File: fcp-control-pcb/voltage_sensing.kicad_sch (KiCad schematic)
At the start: 143 parts, among them J13 Conn_01x10_Male, J14 Conn_01x10_Male, J15 Conn_01x10_Male, U10 LM2902, U11 LM2902, U12 LM2902, U13 CD74HC4067SM, U14 CD74HC4067SM, U5 LM2902, U6 LM2902, U7 LM2902, U8 LM2902, U9 LM2902

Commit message: queen r1.1
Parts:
- removed C13, C14, C15, C16, C17, C18, C19, C20, C21, C22: 0.1 uF, Capacitor_SMD:C_0805_2012Metric_Pad1.18x1.45mm_HandSolder, symbol Device:C
- removed R10, R106, R107, R108, R109, R11, R110, R111, R112, R113, R114, R115, R116, R117, R12, R13, R14, R15, R16, R17, R18, R19, R20, R21, R22, R23, R24, R25, R42, R43, R44, R45, R46, R47, R48, R49, R50, R51, R52, R53, R54, R55, R56, R57, R74, R75, R76, R77, R78, R79, R80, R81, R82, R83, R84, R85, R86, R87, R88, R89: 20k, Resistor_SMD:R_0402_1005Metric_Pad0.72x0.64mm_HandSolder, symbol Device:R
- removed R100, R101, R102, R103, R104, R105, R118, R119, R120, R121, R122, R123, R124, R125, R126, R127, R128, R129, R26, R27, R28, R29, R30, R31, R32, R33, R34, R35, R36, R37, R38, R39, R40, R41, R58, R59, R60, R61, R62, R63, R64, R65, R66, R67, R68, R69, R70, R71, R72, R73, R90, R91, R92, R93, R94, R95, R96, R97, R98, R99: 91k, Resistor_SMD:R_0402_1005Metric_Pad0.72x0.64mm_HandSolder, symbol Device:R
- removed U10, U11, U12, U5, U6, U7, U8, U9: LM2902, Package_SO:SOIC-14_3.9x8.7mm_P1.27mm, symbol Amplifier_Operational:LM2902
- removed U13, U14: CD74HC4067SM, Package_SO:SSOP-24_5.3x8.2mm_P0.65mm, symbol 74xx:CD74HC4067SM
- added C? (x2): (no value), symbol Device:C_Small
- added J?: (no value), symbol Connector:Conn_01x02_Male
- added RN? (x2): (no value), symbol Device:R_Pack08
- added RN? (x3): 3.3k, Package_SO:SOIC-16_4.55x10.3mm_P1.27mm, symbol Device:R_Pack08
- added RN? (x3): 1k, Package_SO:SOIC-16_4.55x10.3mm_P1.27mm, symbol Device:R_Pack08
- added U? (x3): ADC1283, Package_SO:TSSOP-16_4.4x5mm_P0.65mm, symbol Custom:ADC1283
- added U?: (no value), symbol Custom:AS78L05RTR-G1
- added U?: (no value), symbol Custom:ADC1283
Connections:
- net +5V: now also U?.13 (DVCC), U?.13 (DVCC), U?.13 (DVCC), U?.13 (DVCC)
- net GND: now also C?.2, C?.2, U?.12 (DGND), U?.12 (DGND), U?.12 (DGND), U?.2 (GND), U?.3 (AGND), U?.3 (AGND), U?.3 (AGND), U?.3 (AGND)
- net VCC: now also C?.1, U?.3 (IN)
- net at J15.4 (Pin_4): now also RN?.14 (R3.2)
- net at J14.4 (Pin_4): now also RN?.16 (R1.2)
- net at J14.9 (Pin_9): now also RN?.13 (R4.2)
- net at J13.2 (Pin_2): now also RN?.16 (R1.2)
- net at J15.9 (Pin_9): now also RN?.11 (R6.2)
- net at J13.3 (Pin_3): now also RN?.9 (R8.2)
- net at J15.5 (Pin_5): now also RN?.15 (R2.2)
- net at J15.10 (Pin_10): now also RN?.12 (R5.2)
- net at J14.7 (Pin_7): now also RN?.11 (R6.2)
- net at J14.8 (Pin_8): now also RN?.12 (R5.2)
- net at J15.6 (Pin_6): now also RN?.16 (R1.2)
- net at J13.5 (Pin_5): now also RN?.11 (R6.2)
- net at J14.10 (Pin_10): now also RN?.14 (R3.2)
- net at J13.4 (Pin_4): now also RN?.10 (R7.2)
- net at J14.3 (Pin_3): now also RN?.15 (R2.2)
- net at J13.7 (Pin_7): now also RN?.13 (R4.2)
- net at J14.1 (Pin_1): now also RN?.13 (R4.2)
- net at J13.1 (Pin_1): now also RN?.15 (R2.2)
- net at J13.10 (Pin_10): now also RN?.16 (R1.2)
- net at J13.6 (Pin_6): now also RN?.12 (R5.2)
- net at J13.8 (Pin_8): now also RN?.14 (R3.2)
- net at J13.9 (Pin_9): now also RN?.15 (R2.2)
- net at J15.8 (Pin_8): now also RN?.10 (R7.2)
- net at J15.1 (Pin_1): now also RN?.11 (R6.2)
- net at J15.2 (Pin_2): now also RN?.12 (R5.2)
- net at J15.3 (Pin_3): now also RN?.13 (R4.2)
- net at J15.7 (Pin_7): now also RN?.9 (R8.2)
- net at J14.5 (Pin_5): now also RN?.9 (R8.2)
- net at J14.2 (Pin_2): now also RN?.14 (R3.2)
- net at J14.6 (Pin_6): now also RN?.10 (R7.2)
- new net: J?.2 (Pin_2), RN?.10 (R7.2)
- new net: J?.1 (Pin_1), RN?.9 (R8.2)
- new net +5VA: C?.1, U?.1 (OUT), U?.2 (AVCC), U?.2 (AVCC), U?.2 (AVCC), U?.2 (AVCC)
- new net ADCSelect0: U?.1 (CS)
- new net ADCSelect1: U?.1 (CS)
- new net ADCSelect2: U?.1 (CS)
- new net ADCSelect3: U?.1 (CS)
- new net DIN: U?.14 (DIN)
- new net DOUT: U?.14 (DIN), U?.14 (DIN), U?.14 (DIN), U?.15 (DOUT), U?.15 (DOUT), U?.15 (DOUT), U?.15 (DOUT)
- new net SCLK: U?.16 (SCLK), U?.16 (SCLK), U?.16 (SCLK), U?.16 (SCLK)
- new net cell1: RN?.1 (R1.1), RN?.16 (R1.2), U?.4 (IN0)
- new net cell10: RN?.15 (R2.2), RN?.2 (R2.1), U?.5 (IN1)
- new net cell11: RN?.14 (R3.2), RN?.3 (R3.1), U?.6 (IN2)
- new net cell12: RN?.13 (R4.2), RN?.4 (R4.1), U?.7 (IN3)
- new net cell13: RN?.12 (R5.2), RN?.5 (R5.1), U?.8 (IN4)
- new net cell14: RN?.11 (R6.2), RN?.6 (R6.1), U?.9 (IN5)
- new net cell15: RN?.10 (R7.2), RN?.7 (R7.1), U?.10 (IN6)
- new net cell16: RN?.8 (R8.1), RN?.9 (R8.2), U?.11 (IN7)
- new net cell17: RN?.1 (R1.1), RN?.16 (R1.2), U?.4 (IN0)
- new net cell18: RN?.15 (R2.2), RN?.2 (R2.1), U?.5 (IN1)
- new net cell19: RN?.14 (R3.2), RN?.3 (R3.1), U?.6 (IN2)
- new net cell2: RN?.15 (R2.2), RN?.2 (R2.1), U?.5 (IN1)
- new net cell20: RN?.13 (R4.2), RN?.4 (R4.1), U?.7 (IN3)
- new net cell21: RN?.12 (R5.2), RN?.5 (R5.1), U?.8 (IN4)
- new net cell22: RN?.11 (R6.2), RN?.6 (R6.1), U?.9 (IN5)
- new net cell23: RN?.10 (R7.2), RN?.7 (R7.1), U?.10 (IN6)
- new net cell24: RN?.8 (R8.1), RN?.9 (R8.2), U?.11 (IN7)
- new net cell25: RN?.1 (R1.1), RN?.16 (R1.2), U?.4 (IN0)
- new net cell26: RN?.15 (R2.2), RN?.2 (R2.1), U?.5 (IN1)
- new net cell27: RN?.14 (R3.2), RN?.3 (R3.1), U?.6 (IN2)
- new net cell28: RN?.13 (R4.2), RN?.4 (R4.1), U?.7 (IN3)
- new net cell29: RN?.12 (R5.2), RN?.5 (R5.1), U?.8 (IN4)
- new net cell3: RN?.14 (R3.2), RN?.3 (R3.1), U?.6 (IN2)
- new net cell30: RN?.11 (R6.2), RN?.6 (R6.1), U?.9 (IN5)
- new net cell4: RN?.13 (R4.2), RN?.4 (R4.1), U?.7 (IN3)
- new net cell5: RN?.12 (R5.2), RN?.5 (R5.1), U?.8 (IN4)
- new net cell6: RN?.11 (R6.2), RN?.6 (R6.1), U?.9 (IN5)
- new net cell7: RN?.10 (R7.2), RN?.7 (R7.1), U?.10 (IN6)
- new net cell8: RN?.8 (R8.1), RN?.9 (R8.2), U?.11 (IN7)
- new net cell9: RN?.1 (R1.1), RN?.16 (R1.2), U?.4 (IN0)
- new net extra1: RN?.10 (R7.2), RN?.7 (R7.1), U?.10 (IN6)
- new net extra2: RN?.8 (R8.1), RN?.9 (R8.2), U?.11 (IN7)
- no-connect marks 8 -> 0
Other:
- moved on the sheet: J13, J14, J15

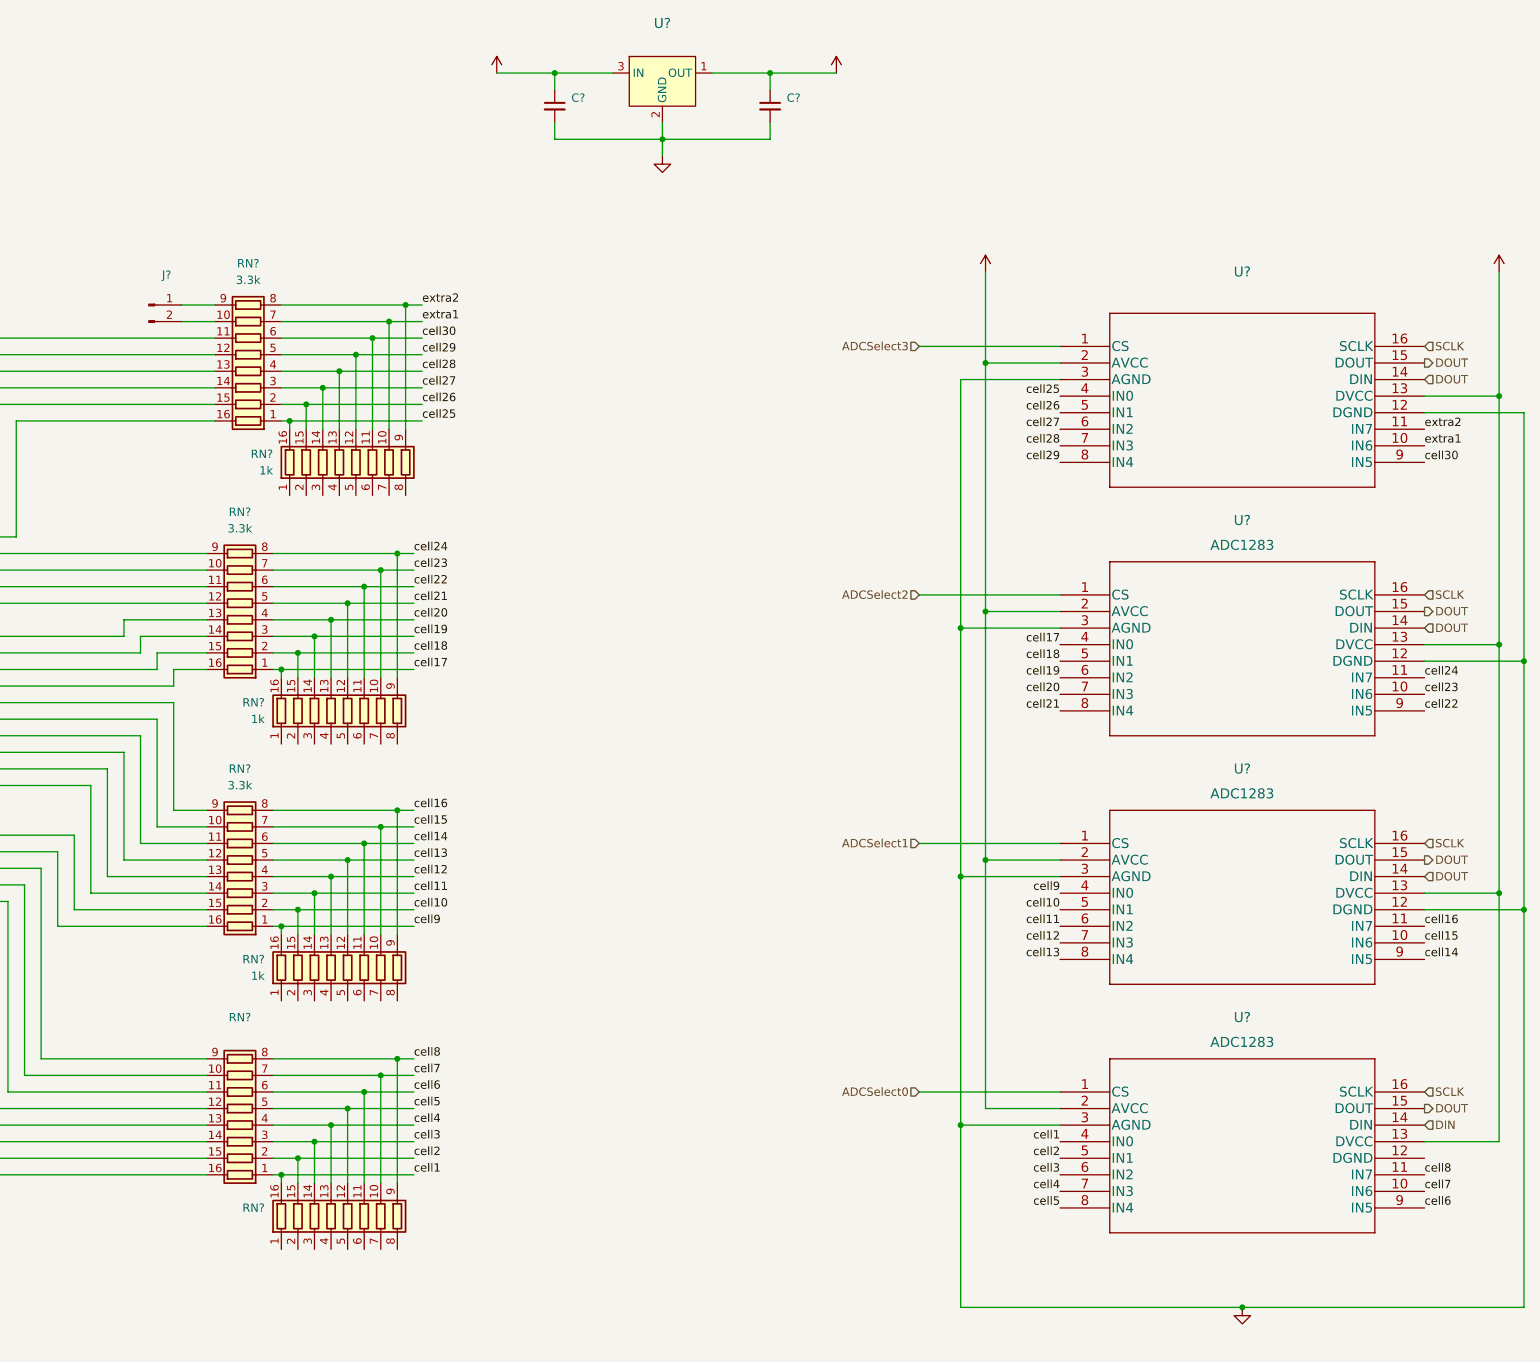
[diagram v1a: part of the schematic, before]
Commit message: Fixed autosave issues
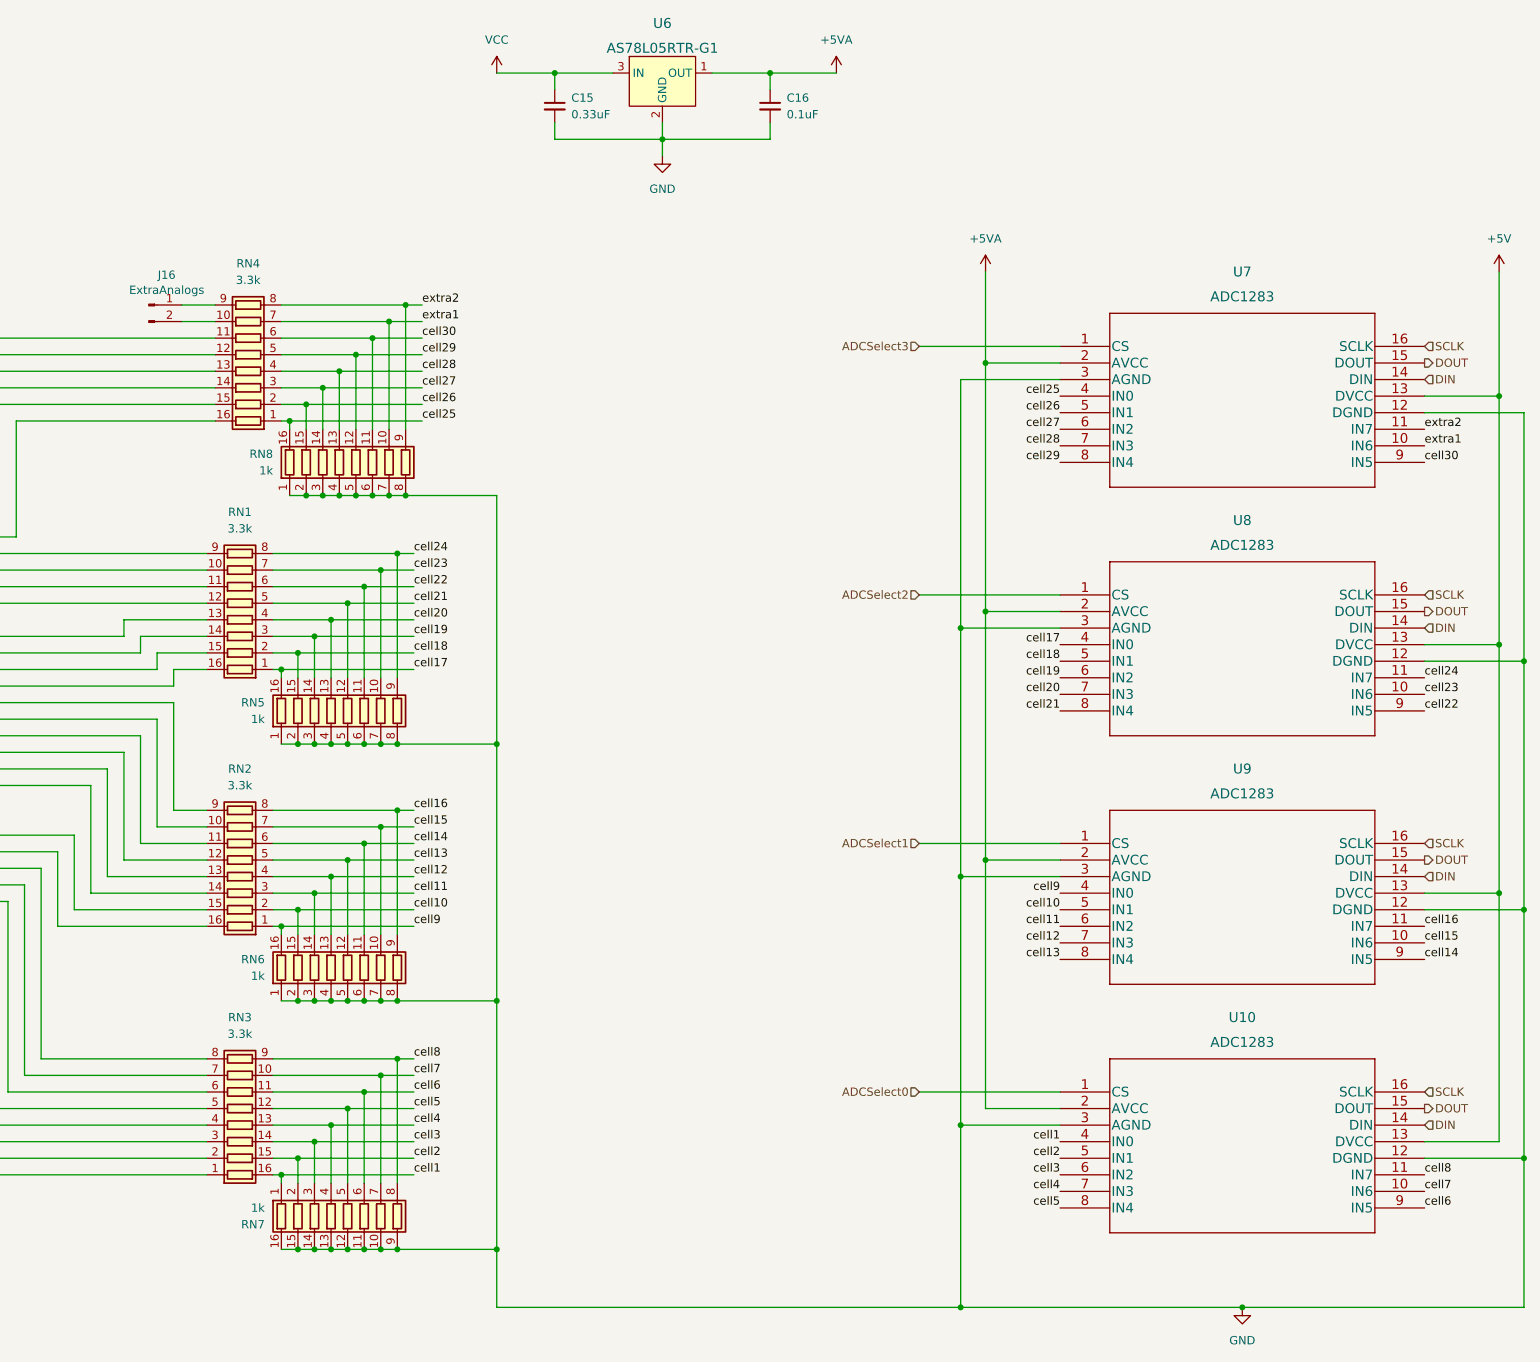
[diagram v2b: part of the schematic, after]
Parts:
- C15: renamed from C?; value (none) -> 0.33uF; footprint (none) -> Capacitor_SMD:C_0805_2012Metric_Pad1.18x1.45mm_HandSolder
- C16: renamed from C?; value (none) -> 0.1uF; footprint (none) -> Capacitor_SMD:C_0805_2012Metric_Pad1.18x1.45mm_HandSolder
- J16: renamed from J?; value (none) -> ExtraAnalogs; footprint (none) -> Connector_PinHeader_2.54mm:PinHeader_1x02_P2.54mm_Vertical
- RN3: renamed from RN?; value (none) -> 3.3k; footprint (none) -> Package_SO:SOIC-16_4.55x10.3mm_P1.27mm
- RN7: renamed from RN?; value (none) -> 1k; footprint (none) -> Package_SO:SOIC-16_4.55x10.3mm_P1.27mm
- U6: renamed from U?; value (none) -> AS78L05RTR-G1; footprint (none) -> Package_TO_SOT_SMD:SOT-89-3_Handsoldering
- U7: renamed from U?; value (none) -> ADC1283; footprint (none) -> Package_SO:TSSOP-16_4.4x5mm_P0.65mm
- gave numbers to parts that had none: 9
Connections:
- net DIN: now also U7.14 (DIN), U8.14 (DIN), U9.14 (DIN)
- net DOUT: no longer U7.14 (DIN), U8.14 (DIN), U9.14 (DIN)
- net GND: now also RN5.1 (R1.1), RN5.2 (R2.1), RN5.3 (R3.1), RN5.4 (R4.1), RN5.5 (R5.1), RN5.6 (R6.1), RN5.7 (R7.1), RN5.8 (R8.1), RN6.1 (R1.1), RN6.2 (R2.1), RN6.3 (R3.1), RN6.4 (R4.1), RN6.5 (R5.1), RN6.6 (R6.1), RN6.7 (R7.1), RN6.8 (R8.1), RN7.10 (R7.2), RN7.11 (R6.2), RN7.12 (R5.2), RN7.13 (R4.2), RN7.14 (R3.2), RN7.15 (R2.2), RN7.16 (R1.2), RN7.9 (R8.2), RN8.1 (R1.1), RN8.2 (R2.1), RN8.3 (R3.1), RN8.4 (R4.1), RN8.5 (R5.1), RN8.6 (R6.1), RN8.7 (R7.1), RN8.8 (R8.1), U10.12 (DGND)
- net cell1: now also RN3.16 (R1.2), RN7.1 (R1.1); no longer RN3.1 (R1.1), RN7.16 (R1.2)
- net cell2: now also RN3.15 (R2.2), RN7.2 (R2.1); no longer RN3.2 (R2.1), RN7.15 (R2.2)
- net cell3: now also RN3.14 (R3.2), RN7.3 (R3.1); no longer RN3.3 (R3.1), RN7.14 (R3.2)
- net cell4: now also RN3.13 (R4.2), RN7.4 (R4.1); no longer RN3.4 (R4.1), RN7.13 (R4.2)
- net cell5: now also RN3.12 (R5.2), RN7.5 (R5.1); no longer RN3.5 (R5.1), RN7.12 (R5.2)
- net cell6: now also RN3.11 (R6.2), RN7.6 (R6.1); no longer RN3.6 (R6.1), RN7.11 (R6.2)
- net cell7: now also RN3.10 (R7.2), RN7.7 (R7.1); no longer RN3.7 (R7.1), RN7.10 (R7.2)
- net cell8: now also RN3.9 (R8.2), RN7.8 (R8.1); no longer RN3.8 (R8.1), RN7.9 (R8.2)
- net at J13.10 (Pin_10): now also RN3.1 (R1.1); no longer RN3.16 (R1.2)
- net at J13.3 (Pin_3): now also RN3.8 (R8.1); no longer RN3.9 (R8.2)
- net at J13.4 (Pin_4): now also RN3.7 (R7.1); no longer RN3.10 (R7.2)
- net at J13.5 (Pin_5): now also RN3.6 (R6.1); no longer RN3.11 (R6.2)
- net at J13.6 (Pin_6): now also RN3.5 (R5.1); no longer RN3.12 (R5.2)
- net at J13.7 (Pin_7): now also RN3.4 (R4.1); no longer RN3.13 (R4.2)
- net at J13.8 (Pin_8): now also RN3.3 (R3.1); no longer RN3.14 (R3.2)
- net at J13.9 (Pin_9): now also RN3.2 (R2.1); no longer RN3.15 (R2.2)
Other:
- moved on the sheet: RN3
